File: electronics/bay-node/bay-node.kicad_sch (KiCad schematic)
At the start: 0 parts

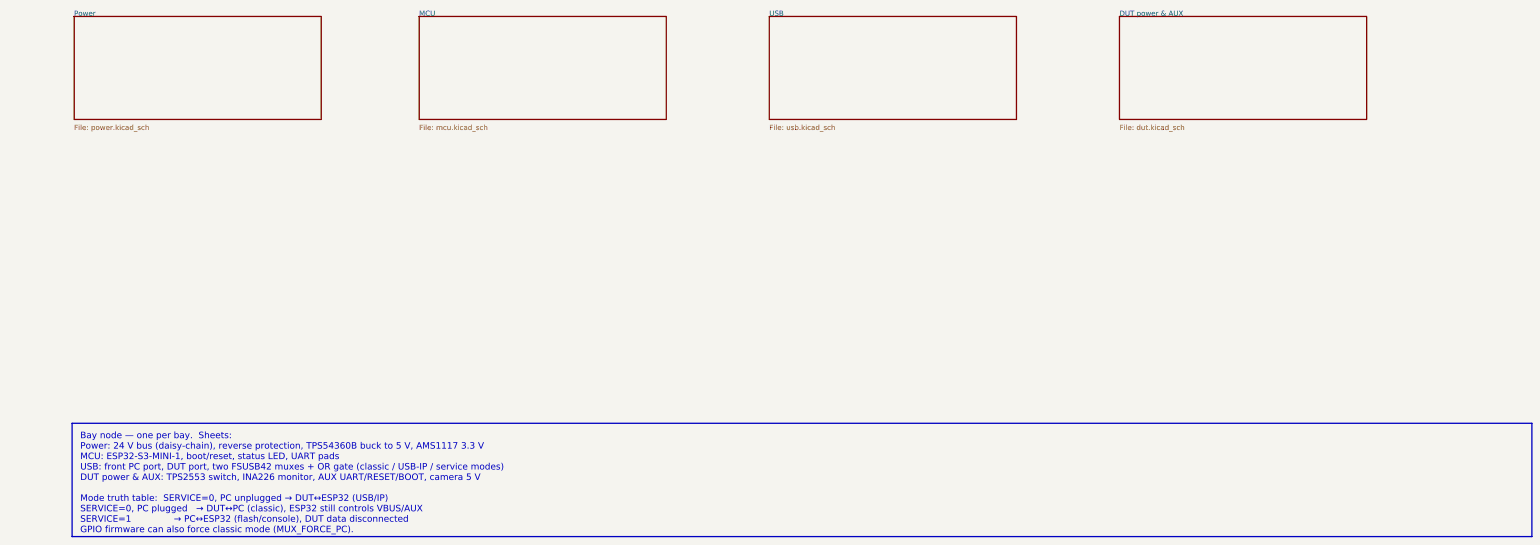
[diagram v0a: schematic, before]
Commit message: Schematics: draw real wires and an overview block diagram
The generator used to connect every pin through a net label only. Now,
in each block, the part with the most pins is the anchor and the
two-pin parts that share a signal with one of its side pins hang off
that pin on a real wire; parts chained behind them (R -> C -> GND)
stack underneath, and anchor-less blocks (pull-ups, reset/boot
buttons) are adopted by the anchor they connect to. Power symbols on
side pins point outward; power-flag references are hidden.

The root sheet becomes a block diagram: the supply rails each sheet
uses across the top, and one lane per pair of sheets listing the
signals they share.

Every wired net still carries one label, so net names, ERC (0) and the
PCB's schematic parity (0) are unchanged; the routed PCBs are untouched.

Co-Authored-By: Claude Opus 5.5 <noreply@anthropic.com>
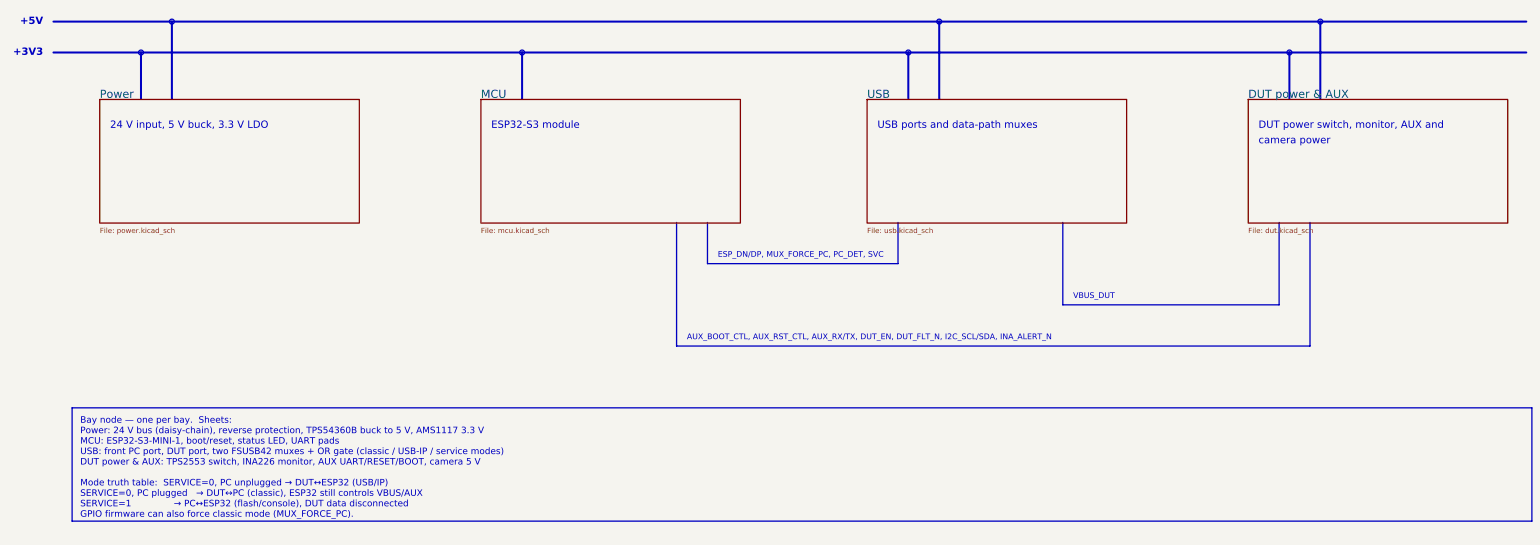
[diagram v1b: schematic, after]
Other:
- note added: "+3V3"
- note added: "+5V"
- note added: "24 V input, 5 V buck, 3.3 V LDO"
- note added: "AUX_BOOT_CTL, AUX_RST_CTL, AUX_RX/TX, DUT_EN, DUT_FLT_N, I2C_SCL/SDA, INA_ALERT_N"
- note added: "DUT power switch, monitor, AUX and"
- note added: "ESP32-S3 module"
- note added: "ESP_DN/DP, MUX_FORCE_PC, PC_DET, SVC"
- note added: "USB ports and data-path muxes"
- note added: "VBUS_DUT"
- note added: "camera power"

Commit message: Boards v0.2: LMR51635 buck, JST PH, drawn schematics, thermal reliefs
Addresses Fabio's review of v0.1.

Bay node (rev 0.2):
- 5 V buck: LMR51635YDDCR (60 V, 3.5 A, synchronous, 1.1 MHz) with a
  3.3 uH FXL0630, 3 x 22 uF out, 2 x 10 uF + 100 nF in, FB 120k/22k
  (5.16 V), EN 1M/100k UVLO (13.5 V on, 10.8 V off). Replaces the
  TPS54360B, its Schottky and compensation network. CIN straddles the
  VIN/GND pins on solid top-side islands with vias to In1 (TI SLUSF64B).
- 24 V in/out on JST PH (carrier notches resized, rack.yaml pwr_y).
- Power nets named along the path: 24V_BUS -> +24V -> +5V -> DUT_5V_SW
  -> shunt -> DUT_5V; the INA226 visibly runs from +3V3.
- Stackup S+GND / GND / PWR / S+GND: In2 carries +5V, +3V3 under the
  ESP32 and a protected 24 V bus strip. Outer GND pours kept (without
  them Freerouting left ~25 connections unrouted).

Power hub (rev 0.2): JST VH input instead of the screw terminal, JST PH
row outputs, eFuse limit 1.6 A (RILIM 7.5k) to protect the 2 A contacts.

Generator:
- eda.py: drawn schematic mode (sch= placement, Sheet.wire/tag/frame,
  rotated/mirrored symbols, automatic junctions, per-island labels and
  checks that no wire touches another net); all seven sheets redrawn.
- pcbgen.py: thermal reliefs on every pour (+ <board>.kicad_dru for
  single spokes on fine pitch), configurable inner layers, per-zone
  deferral, fixed vias, DRC-driven fix-up for isolated GND pads.
- JLC CPL fix for the LMR51635 (270 deg); BOM, cables, viewer, docs.

ERC 0, DRC 0 copper errors, 0 unconnected, schematic parity 0 on both.

Co-Authored-By: Claude Opus 5.5 <noreply@anthropic.com>
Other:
- note added: "DUT_5V"
- note removed: "VBUS_DUT"
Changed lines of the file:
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@@
 	(title_block
 		(title "Bay node — Overview")
-		(rev "0.1")
+		(rev "0.2")
 		(company "hw-testing-rack")
 		(comment 1 "ESP32-S3 USB/IP host for one bay of the hw-testing-rack shelf")
@@
 		)
 	)
-	(text "VBUS_DUT"
+	(text "DUT_5V"
 		(exclude_from_sim no)
 		(at 276.86 119.38 0)
@@
 		)
 	)
-	(text_box "Bay node — one per bay.  Sheets:\n  Power: 24 V bus (daisy-chain), reverse protection, TPS54360B buck to 5 V, AMS1117 3.3 V\n  MCU: ESP32-S3-MINI-1, boot/reset, status LED, UART pads\n  USB: front PC port, DUT port, two FSUSB42 muxes + OR gate (classic / USB-IP / service modes)\n  DUT power & AUX: TPS2553 switch, INA226 monitor, AUX UART/RESET/BOOT, camera 5 V\n\nMode truth table:  SERVICE=0, PC unplugged → DUT↔ESP32 (USB/IP)\n                   SERVICE=0, PC plugged   → DUT↔PC (classic), ESP32 still controls VBUS/AUX\n                   SERVICE=1               → PC↔ESP32 (flash/console), DUT data disconnected\nGPIO firmware can also force classic mode (MUX_FORCE_PC)."
+	(text_box "Bay node — one per bay.  Sheets:\n  Power: 24 V bus (JST PH daisy chain), reverse protection, LMR51635 buck to 5 V, AMS1117 3.3 V\n  MCU: ESP32-S3-MINI-1, reset/boot, status LED, UART pads\n  USB: front PC port, DUT port, two FSUSB42 muxes + OR gate (classic / USB-IP / service modes)\n  DUT power & AUX: TPS2553 switch → shunt → DUT_5V, INA226 monitor, AUX UART/RESET/BOOT, camera 5 V\n\nMode truth table:  SERVICE=0, PC unplugged → DUT↔ESP32 (USB/IP)\n                   SERVICE=0, PC plugged   → DUT↔PC (classic), ESP32 still controls DUT_5V/AUX\n                   SERVICE=1               → PC↔ESP32 (flash/console), DUT data disconnected\nGPIO firmware can also force classic mode (MUX_FORCE_PC)."
 		(exclude_from_sim no)
 		(at 30 146.05 0)

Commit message: Bay node v0.5: 6-pin row cable with CAN and POS
The row cable becomes the docs/can.md contract: J1 (ROW IN, left) and J2 (ROW OUT,
right) are 6-pin JST PH S6B-PH-SM4-TB, +24 V, GND, CAN_H, CAN_L, GND, POS, with
pin 1 to the rear on the left edge and to the front on the right edge.

- Rack bus sheet: TCAN1044AV (VCC 5 V, VIO 3.3 V, STB low) right on the pair,
  which runs straight J1 -> J2 with no termination (stubs 1.8 / 2.3 mm),
  PESD2CAN on the tap; POS in through 10k + BAT54S + 100k pull-down, POS out
  through 10k + BAT54S.  TWAI on IO18/IO17, POS on IO16 (in) and IO35 (out).
- The input stage also takes a 20 / 28 V USB-C PD supply (notes on the Power
  sheet and in docs/electronics.md).
- Re-placed for In2 power only and autorouted: ERC 0, DRC 0, unconnected 0,
  parity 0 (kicad-cli and Konnect); no track on In1 or In2.
- JLC_CPL_FIX gains the rack bus parts, fitted on the EasyEDA footprints:
  S6B 180 deg, TCAN1044AV 270 deg, PESD2CAN and BAT54S 180 deg (they also apply
  to the power hub's row connectors, transceiver and clamps).
- Firmware: hwtr,rack-bus binding, TWAI pinctrl and node in the bay_node
  devicetree, check_pinmap and the README table; DevKitC moves POS_OUT to IO21,
  StampS3 disables the bus.  bay_node, DevKitC and StampS3 builds pass.
- Mechanics: the cable windows in the tray walls and the ladders widen to
  17 mm for the PHR-6 plug.  The viewer and the notice draw a 6-wire jumper.
- BOM: 6-pin jumpers; JLC_SINCE_QUOTE adds rev 0.5's parts and three extended
  part types to the node's quoted order (indicative, re-quote).

Regenerated: KiCad project, fab outputs, renders, schematic PDF, viewer GLB,
tray and ladder STLs, parts.glb, rack.json, bom/*.

Co-Authored-By: Claude Opus 5.5 <noreply@anthropic.com>
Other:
- added sheet Rack bus (bus.kicad_sch)
- note added: "CAN_H/L, POS_IN_CONN, POS_OUT_CONN"
- note added: "CAN_RXD/TXD, POS_IN/OUT"
- note added: "Rack bus: CAN transceiver and POS"
- note added: "addressing token"

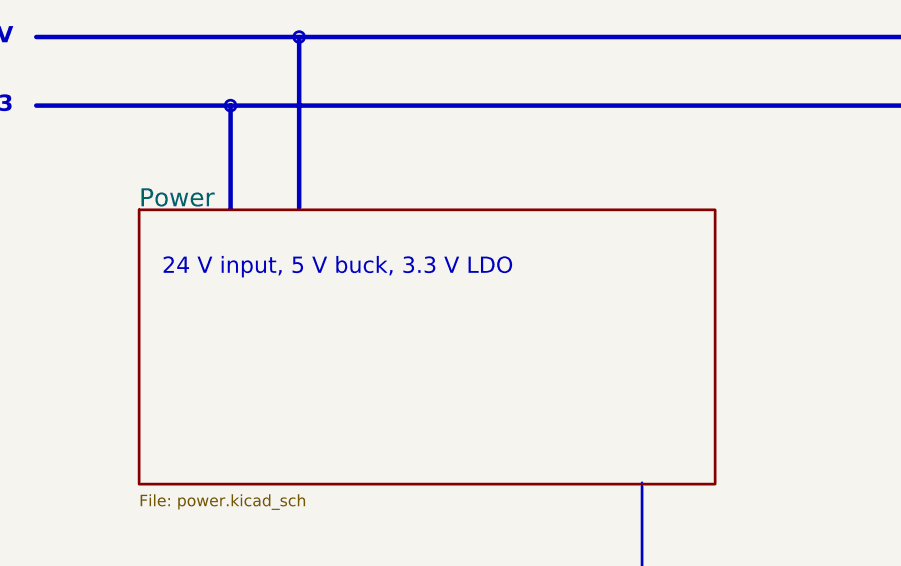
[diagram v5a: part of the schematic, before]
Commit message: Bay node v0.5: VRACK, GCT USB-C, VBUS caps on the ESD parts
Follows the power box's switch to USB-C PD (docs/can.md on the power-box branch):

- Pin 1 of the row cable is VRACK (20 V, or 28 V EPR): the net 24V_BUS becomes
  VRACK and +24V (after the P-FET) becomes VIN, in the schematic, the zones and
  the netclass patterns.  The input stage already takes 20-28 V.
- J3/J4 become the GCT USB4105-GF-A-120 (catalog usbc5a, LCSC C5184243), the
  part the user approved for the hub.  KiCad 10 ships its 3D model.  The pads
  sit 0.365 mm closer to the footprint origin than the HRO's, so the hand-drawn
  USB High-Speed tracks move with them (both lines of each pair alike, so the
  matching holds).  A board rule allows the footprint's own 0.19 mm between its
  GND pads and its pegs, the same rule the hub uses.
- Konnect's open point from v0.4: C25 and C26 (100 nF) on U4's and U8's VBUS.
- JLC_CPL_FIX: C5184243 at 0 deg, -1.30 mm y (EasyEDA fit, residual 0).
- JLC_SINCE_QUOTE: +$2.38 of parts per board ($38.10 for the 16 quoted).

ERC 0, DRC 0, unconnected 0, parity 0; Konnect's design review shows only the
known per-sheet false positives.  CAN stubs to U11: 2.2 / 7.9 mm.

Co-Authored-By: Claude Opus 5.5 <noreply@anthropic.com>
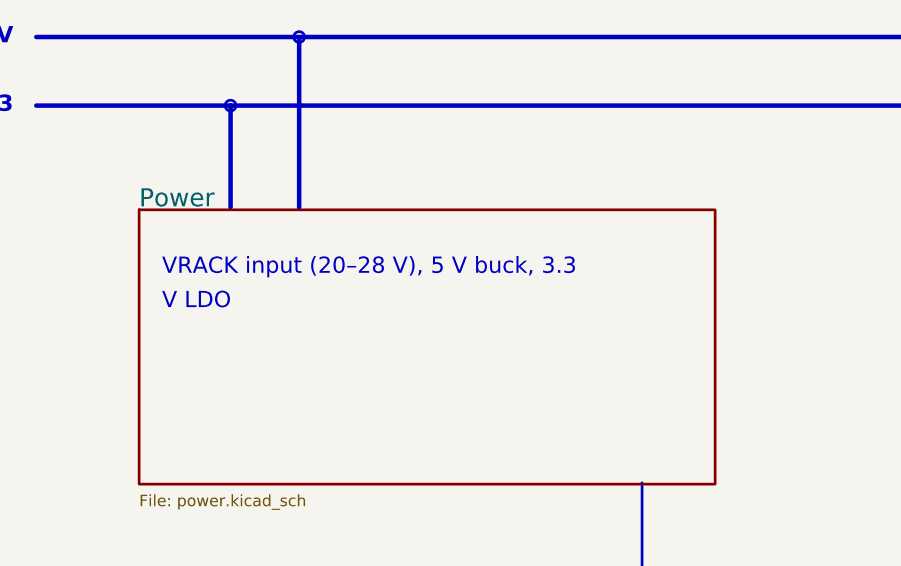
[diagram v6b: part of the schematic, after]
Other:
- note added: "V LDO"
- note added: "VRACK input (20–28 V), 5 V buck, 3.3"
- note removed: "24 V input, 5 V buck, 3.3 V LDO"
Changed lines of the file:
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@@
 		)
 	)
-	(text "24 V input, 5 V buck, 3.3 V LDO"
+	(text "VRACK input (20–28 V), 5 V buck, 3.3"
 		(exclude_from_sim no)
 		(at -8.89 77.47 0)
 		(effects
 			(font
+				(size 1.8 1.8)
+			)
+			(justify left bottom)
+		)
+	)
+	(text "V LDO"
+		(exclude_from_sim no)
+		(at -8.89 81.28 0)
+		(effects
+			(font

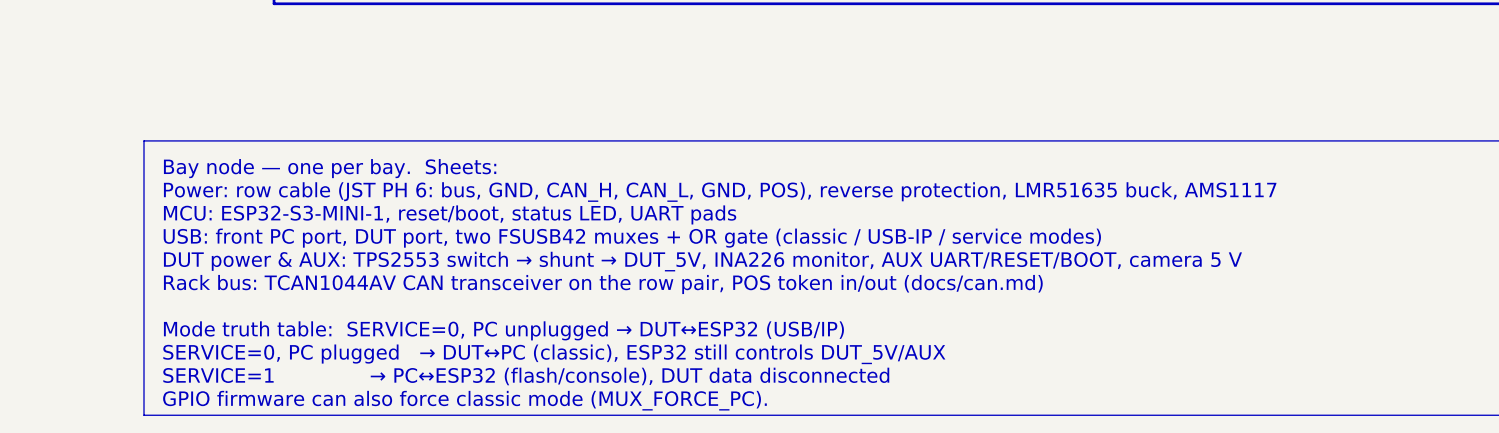
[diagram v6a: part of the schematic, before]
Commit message: CAN transceiver: TCAN1462V (signal improvement) on the hub and the bay node
Same SOIC-8 pinout as the TCAN1044AV (VIO on pin 5, STB on pin 8), so the
footprint, placement and routing are unchanged: the regenerated PCBs keep
every track and via, only U6 / U11's value and fields change.  Signal
improvement (CiA 601-4, ISO 11898-2:2024 set C) damps the ringing of the
star's open branch ends; the termination (56 ohm at the hub) stays.

* catalog: TCAN1462VDRQ1 (C7399456, no LCSC stock on 2026-10-18), with the
  TCAN1044AVDRQ1 (C3234993) and NXP TJA1462AT/0Z (C3234095) as alternates;
  CPL rotation for all three.
* BOM: the board BOMs' alternates now show in the rack BOM notes; JLC
  estimates +$0.54 per board.
* docs/can.md: why the star is fine at 250 kbit/s and what SIC adds, with
  sources (TI SLLSFF2B, SLLA581A; CiA bit-timing table; NXP TJA1462).
* Both boards: ERC 0, DRC 0 errors, 0 unconnected, parity 0; 3D 0 stand-ins.

Co-Authored-By: Claude Opus 5.5 <noreply@anthropic.com>
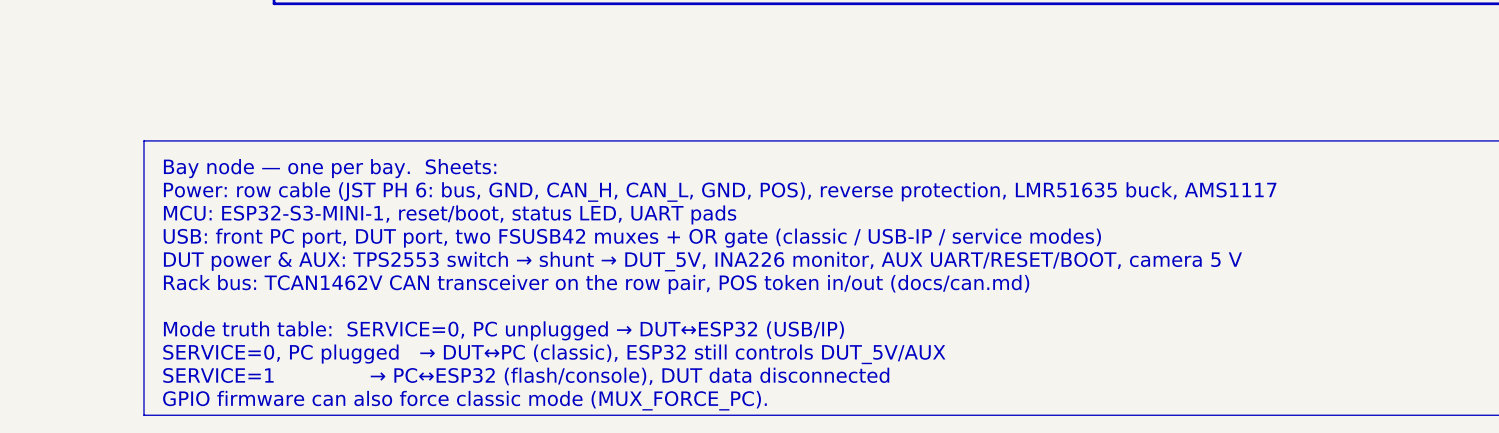
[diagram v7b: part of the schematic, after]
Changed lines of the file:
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@@
 		)
 	)
-	(text_box "Bay node — one per bay.  Sheets:\n  Power: row cable (JST PH 6: bus, GND, CAN_H, CAN_L, GND, POS), reverse protection, LMR51635 buck, AMS1117\n  MCU: ESP32-S3-MINI-1, reset/boot, status LED, UART pads\n  USB: front PC port, DUT port, two FSUSB42 muxes + OR gate (classic / USB-IP / service modes)\n  DUT power & AUX: TPS2553 switch → shunt → DUT_5V, INA226 monitor, AUX UART/RESET/BOOT, camera 5 V\n  Rack bus: TCAN1044AV CAN transceiver on the row pair, POS token in/out (docs/can.md)\n\nMode truth table:  SERVICE=0, PC unplugged → DUT↔ESP32 (USB/IP)\n                   SERVICE=0, PC plugged   → DUT↔PC (classic), ESP32 still controls DUT_5V/AUX\n                   SERVICE=1               → PC↔ESP32 (flash/console), DUT data disconnected\nGPIO firmware can also force classic mode (MUX_FORCE_PC)."
+	(text_box "Bay node — one per bay.  Sheets:\n  Power: row cable (JST PH 6: bus, GND, CAN_H, CAN_L, GND, POS), reverse protection, LMR51635 buck, AMS1117\n  MCU: ESP32-S3-MINI-1, reset/boot, status LED, UART pads\n  USB: front PC port, DUT port, two FSUSB42 muxes + OR gate (classic / USB-IP / service modes)\n  DUT power & AUX: TPS2553 switch → shunt → DUT_5V, INA226 monitor, AUX UART/RESET/BOOT, camera 5 V\n  Rack bus: TCAN1462V CAN transceiver on the row pair, POS token in/out (docs/can.md)\n\nMode truth table:  SERVICE=0, PC unplugged → DUT↔ESP32 (USB/IP)\n                   SERVICE=0, PC plugged   → DUT↔PC (classic), ESP32 still controls DUT_5V/AUX\n                   SERVICE=1               → PC↔ESP32 (flash/console), DUT data disconnected\nGPIO firmware can also force classic mode (MUX_FORCE_PC)."
 		(exclude_from_sim no)
 		(at 30 166.37 0)

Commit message: Bay node: the bay's camera on J6, the WROOM-1-N8R8, the board 64 × 90
The user chose a camera per bay wired to its own node (camera hand-over,
option B: an Arducam Mega 3MP SPI, M12 ≈ 120°, and white LEDs on one PH 8
lead) and the ESP32-S3-WROOM-1-N8R8 for its 8 MB octal PSRAM, allowing
the board to grow at the rear.

- U3: WROOM-1-N8R8 (C2913201), the DevKitC-1-N8R8's module.  The board
  grew 10 mm at the rear (64 × 90): the layout, the holes and every
  pcb.bay_node y moved 10 mm with it, so the tray's standoffs and the
  fascia parts keep their place; the module's top edge is the new rear
  edge, its antenna band (6 mm, ±24 mm) kept clear.  bench footprint
  ESP32-S3-WROOM-1_NoEPVias: the stock one without its 0.2 mm in-pad
  vias, the pad on a GND island stitched around it.
- Pin map (the PSRAM takes IO35–37, no IO26/33/34 on a WROOM-1), the
  DevKitC-1 v1.1's as is: IO1/IO2 I²C, IO12 AUX_RST, IO21 AUX_RX, IO38 LED,
  IO42 POS_OUT; camera IO11 SCK, IO10 MOSI, IO9 MISO, IO8 CS, IO7 light.
- J6: PH 8 vertical (B8B) right of the PC pair, under J7; 33 Ω series,
  2 × USBLC6, CS 10k pull-up, MISO divider footprint (R35 DNP), the light
  on an AO3400A (100k gate pull-down), CAM_5V through the PTC.  A
  "Camera" schematic sheet.
- J5 (AUX): a vertical PH 6 (B6B), as the user asked.
- Re-routed.  ERC 0, DRC 0 / 0 unconnected / parity 0, JLC DFM: only the
  back-side test pads, 97/97 3D models (the B6B's EasyEDA STEP is not
  centred and turned).  The session import now also drops a via at the
  end of a dead branch, and the branch.  JLC corrections fitted for
  C2913201, C495548, C471518, C20917.
- BOM: the camera lines (B0434, 120° lens, LED strip, PH 8 lead) replace
  the XIAO / OV2640 / PH 2 lead; the node's post-quote changes +$18.91
  of parts, +$3 for the B6B type, +$1.83 for the larger board.
- firmware/README.md pin map: the new map.  check_pinmap waits for the
  firmware's devicetree (moved pins, camera).

Co-Authored-By: Claude Opus 5.5 <noreply@anthropic.com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
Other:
- added sheet Camera (cam.kicad_sch)
- note added: "CAM_CS/LED/SCK, CAM_MISO, CAM_MOSI"
- note added: "Camera lead: Arducam Mega SPI and"
- note added: "DUT power switch, monitor and AUX"
- note added: "its LEDs"
- note removed: "DUT power switch, monitor, AUX and"
- note removed: "camera power"
